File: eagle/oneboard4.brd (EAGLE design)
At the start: 43.1 x 58.5 mm, 5 parts

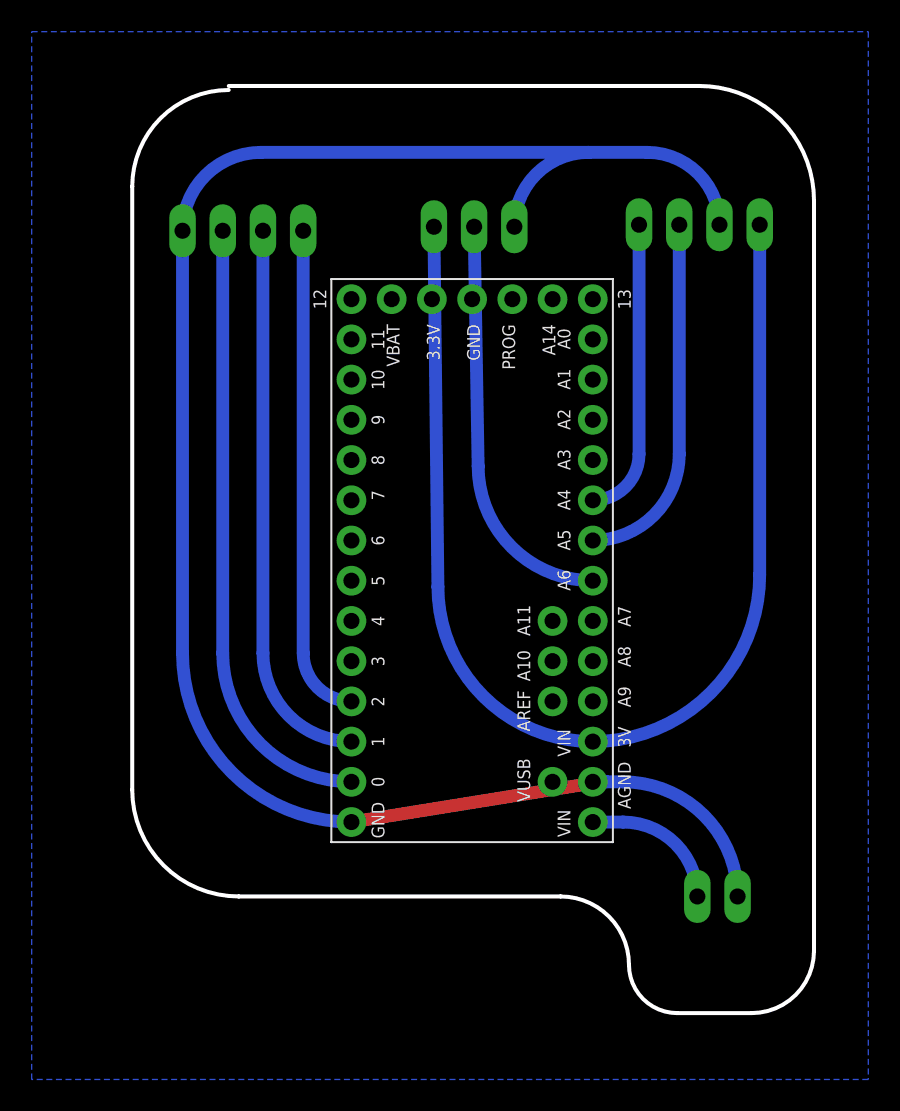
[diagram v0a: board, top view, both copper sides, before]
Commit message: updated eagle board and arduino code
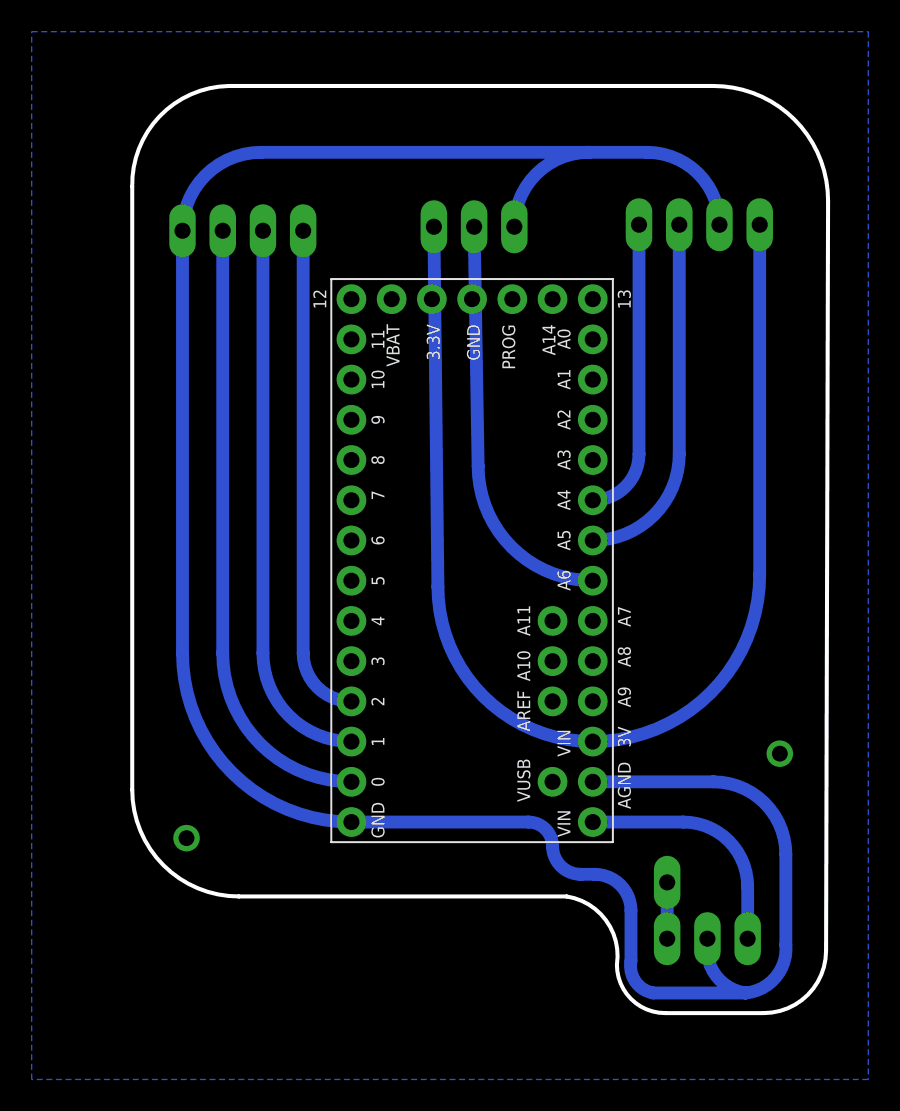
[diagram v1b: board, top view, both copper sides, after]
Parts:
- added U$1: HEADER-3, homemade-hardware:HEADER-3
- U$3: value HEADER-2 -> HEADER-1; device homemade-hardware:HEADER-2 -> homemade-hardware:HEADER-1
- moved U$3 2.10 mm to (40.3, 22.2), turned to 90 degrees
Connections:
- new net N$6: U$1.3, U$3.1
- net GND: now also U$1.2; no longer U$3.2
- net VIN: now also U$1.1; no longer U$3.1
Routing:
- net GND: track 115.7 -> 145.7 mm
- net VIN: track 8.55 -> 14.8 mm
- net N$6: track 0.00 -> 3.56 mm
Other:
- board size 43.1 x 58.5 mm -> 43.9 x 58.5 mm
